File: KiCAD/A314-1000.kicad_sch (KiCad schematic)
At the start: 89 parts, among them IC1 T8Q144xx, IC2 SN74CBTD3384CPWR, IC3 SN74CBTD3384CPWR, IC4 SN74CBTD3384CPWR, IC5 SN74CBTD3384CPWR, IC6 IS61WV12816EDBLL-10TLI, IC7 LM1117MP-1.2, IC8 LM1117MP-3.3, J1 Raspberry_Pi_2_3, J2 2x30 Card edge conn., J3 Conn_01x01, J4 JTAG, Q1 2N7002, Q2 2N7002, U6 W25Q80DVSN, U7 TLV62569P, U8 TLV62569P, X1 25MHz

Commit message: Ready for production?
Board finished, added a RTC for the RPi. With a little luck and some production files, this may be ready for some PCBA :)
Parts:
- removed R3: 442k, Resistor_SMD:R_0603_1608Metric, symbol Device:R
- added BT1: CR2032, A314-1000:BATHLD001, symbol Device:Battery_Cell
- added C47: 100n, Capacitor_SMD:C_0603_1608Metric, symbol Device:C
- added C48, C49: 8p, Capacitor_SMD:C_0402_1005Metric_Pad0.74x0.62mm_HandSolder, symbol Device:C
- added FID1, FID2, FID3: Fiducial, Fiducial:Fiducial_1mm_Mask2mm, symbol Mechanical:Fiducial
- added IC11: PT7C4311WEX, Package_SO:SOIC-8_3.9x4.9mm_P1.27mm, symbol PT7C4311:PT7C4311
- added R17, R23: 3k9, Resistor_SMD:R_0603_1608Metric, symbol Device:R
- added Y1: 32.768kHz, Crystal:Crystal_DS26_D2.0mm_L6.0mm_Horizontal_1EP_style2, symbol Device:Crystal_GND3_Small
- J3: value Conn_01x01 -> INT2
- renumbered U6 to IC12
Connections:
- net INT2 is gone; now on an unnamed net: Q1.1 (G)
- net +3V3: now also C47.1, IC11.8 (V_{cc}), R17.2, R23.2
- net GND: now also BT1.2 (-), C47.2, C48.2, C49.2, IC11.4 (GND), Y1.3
- net JTAG_OE_{0}: now also J1.5 (SCL/GPIO3); no longer J1.37 (GPIO26)
- net JTAG_OE_{1}: now also J1.3 (SDA/GPIO2); no longer J1.13 (GPIO27)
- net PIACK: now also IC1.100 (GPIOR_113/CDI22); no longer IC1.101 (GPIOR_112/CDI23)
- net PIA_{0}: now also IC1.101 (GPIOR_112/CDI23), J1.18 (GPIO24); no longer IC1.111 (GPIOR_85), J1.27 (ID_SD/GPIO0)
- net PIA_{1}: now also IC1.103 (GPIOR_104/CDI25), J1.22 (GPIO25); no longer IC1.110 (GPIOR_87/CDI29), IC5.20 (2B4), J1.28 (ID_SC/GPIO1)
- net PIA_{2}: now also IC1.118 (GPIOR_79/ExtFB1/CDI30), J1.37 (GPIO26); no longer IC1.89 (GPIOR_129/CTRL10), J1.3 (SDA/GPIO2)
- net PIA_{3}: now also IC1.98 (GPIOR_117/CTRL14), J1.13 (GPIO27); no longer IC1.90 (GPIOR_128/CTRL11), J1.5 (SCL/GPIO3)
- net PID_{0}: now also IC1.90 (GPIOR_128/CTRL11); no longer IC1.93 (GPIOR_123/CLK12/CDI20)
- net PID_{10}: now also IC1.89 (GPIOR_129/CTRL10); no longer IC1.92 (GPIOR_125/CLK10)
- net PID_{11}: now also IC1.92 (GPIOR_125/CLK10); no longer IC1.97 (GPIOR_122/CLK13/CDI21)
- net PID_{12}: now also IC1.115 (GPIOR_82); no longer IC1.116 (GPIOR_81/MrefCLK)
- net PID_{13}: now also IC1.97 (GPIOR_122/CLK13/CDI21); no longer IC1.99 (GPIOR_116/CTRL15)
- net PID_{14}: now also IC1.93 (GPIOR_123/CLK12/CDI20); no longer IC1.98 (GPIOR_117/CTRL14)
- net PID_{15}: now also IC1.116 (GPIOR_81/MrefCLK); no longer IC1.117 (GPIOR_80)
- net PID_{1}: now also IC1.111 (GPIOR_85), IC5.20 (2B4); no longer IC1.112 (GPIOR_86)
- net PID_{2}: now also IC1.113 (GPIOR_84); no longer IC1.114 (GPIOR_83)
- net PID_{3}: now also IC1.110 (GPIOR_87/CDI29); no longer IC1.109 (GPIOR_88/CDI28)
- net PID_{4}: now also IC1.106 (GPIOR_94/CDI27); no longer IC1.105 (GPIOR_95/CDI26)
- net PID_{5}: now also IC1.105 (GPIOR_95/CDI26); no longer IC1.103 (GPIOR_104/CDI25)
- net PID_{7}: now also IC1.109 (GPIOR_88/CDI28); no longer IC1.106 (GPIOR_94/CDI27)
- net PID_{8}: now also IC1.112 (GPIOR_86); no longer IC1.113 (GPIOR_84)
- net PID_{9}: now also IC1.114 (GPIOR_83); no longer IC1.115 (GPIOR_82)
- net PIIRQ: now also IC1.99 (GPIOR_116/CTRL15); no longer IC1.100 (GPIOR_113/CDI22)
- net PIWR: now also IC1.117 (GPIOR_80); no longer IC1.118 (GPIOR_79/ExtFB1/CDI30)
- net 1V2PG: now reaches R6.1, U7.1 (EN), U8.5 (PG)
- new net: BT1.1 (+), IC11.3 (V_{bat})
- new net: C49.1, IC11.1 (X1), Y1.1
- new net: C48.1, IC11.2 (X2), Y1.2
- new net: IC11.5 (SDA), J1.27 (ID_SD/GPIO0), R17.1
- new net: IC11.6 (SCL), J1.28 (ID_SC/GPIO1), R23.1
- no-connect marks 11 -> 12
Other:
- moved on the sheet: C1, C12, C2, C3, C4, J3, Q1

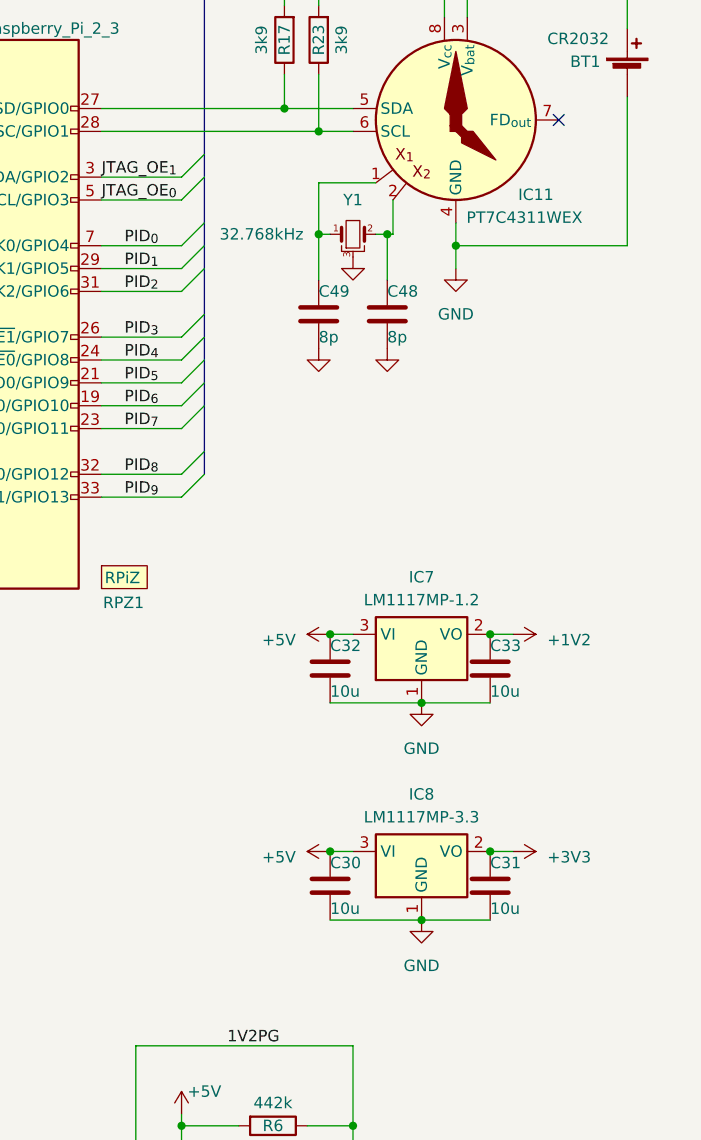
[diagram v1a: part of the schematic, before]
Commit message: Simplified PSU
Enhanced battery replacement ergonomics
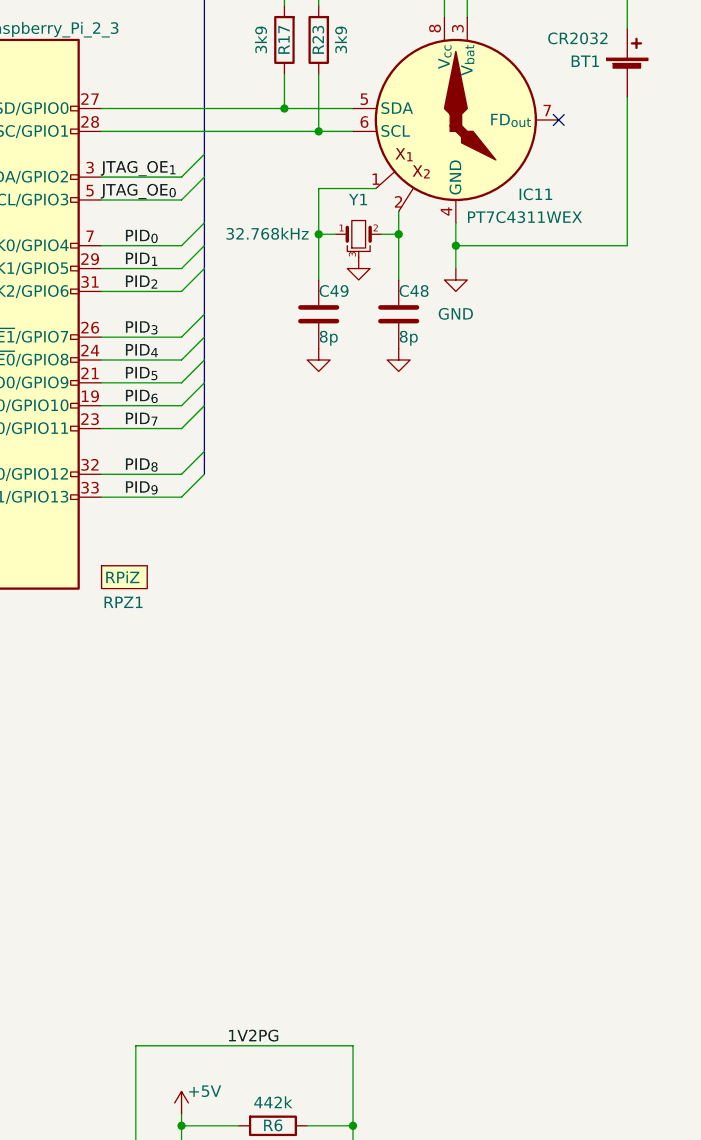
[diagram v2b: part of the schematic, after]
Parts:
- removed C30, C31, C32, C33: 10u, Capacitor_SMD:C_0603_1608Metric_Pad1.08x0.95mm_HandSolder, symbol Device:C
- removed IC7: LM1117MP-1.2, Package_TO_SOT_SMD:SOT-223-3_TabPin2, symbol a314-1000_components:LM1117MP-1.2
- removed IC8: LM1117MP-3.3, Package_TO_SOT_SMD:SOT-223-3_TabPin2, symbol Regulator_Linear:LM1117MP-3.3
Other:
- moved on the sheet: C48, Y1

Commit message: First bug-ridded release
This is the first non-alpha release. The hardware issues that were found in the alpha have been addressed. This board is now sent for a second production run.
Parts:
- added H1, H2: MountingHole, A314-1000:M2.5_Mount, symbol Mechanical:MountingHole
- added J5: RASP_I2C, Connector_PinHeader_2.54mm:PinHeader_1x05_P2.54mm_Vertical, symbol Connector_Generic:Conn_01x05
- added R24: 10k, Resistor_SMD:R_0603_1608Metric, symbol Device:R
- added R25: 3k9, Resistor_SMD:R_0603_1608Metric, symbol Device:R
- BT101: renamed from BT1; LCSC Part # (none) -> C964833
- C1, C10, C11, C12, C13, C14, C15, C16, C17, C18, C19, C2, C20, C21, C22, C23, C24, C25, C26, C27, C28, C29, C3, C4, C44, C45, C46, C5, C6, C7, C8, C9: LCSC Part # (none) -> C14663
- C10, C11, C12, C15, C16, C17: LCSC Part # (none) -> C19702
- C101: renamed from C48; LCSC Part # (none) -> C130118
- C102: renamed from C49; LCSC Part # (none) -> C130118
- C103: renamed from C47; LCSC Part # (none) -> C14663
- C13, C14: LCSC Part # (none) -> C19666
- FID1, FID2, FID3, J2: now left out of the parts list
- IC1: LCSC Part # (none) -> C5246494
- IC101: renamed from IC11; LCSC Part # (none) -> C780886
- IC12: LCSC Part # (none) -> C115408
- IC2, IC3, IC4, IC5: LCSC Part # (none) -> C2674525
- IC6: LCSC Part # (none) -> C1351846
- J1: LCSC Part # (none) -> C2685112
- J3: LCSC Part # (none) -> C2685179
- J4: now not fitted; now left out of the parts list
- L1, L2: LCSC Part # (none) -> C2847469
- Q1, Q2: LCSC Part # (none) -> C8545
- R1: value 6 x 10k -> 10k; LCSC Part # (none) -> C304474
- R10, R11, R12, R13, R14, R15, R2, R3, R4, R5, R6, R8, R9: LCSC Part # (none) -> C304474
- R17, R23: LCSC Part # (none) -> C103605
- R4, R6: LCSC Part # (none) -> C101050
- R4: LCSC Part # (none) -> C144686
- R5, R7, R8: LCSC Part # (none) -> C912480
- R7: value 4 x 10k -> 10k; LCSC Part # (none) -> C304474
- RPZ1: now not fitted
- U7, U8: LCSC Part # (none) -> C398365
- X1: LCSC Part # (none) -> C254248
- Y101: renamed from Y1; LCSC Part # (none) -> C511702
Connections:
- net +3V3: now also J5.2 (Pin_2), R24.2
- net +5V: now also J5.5 (Pin_5)
- net GND: now also J5.1 (Pin_1), R25.1
- net SPI_SS: now also R24.1
- net ~{CRESET}: now also U7.5 (PG)
- net SDA: now reaches IC101.5 (SDA), J1.27 (ID_SD/GPIO0), R17.1
- net SDA: now also J5.4 (Pin_4)
- net SCL: now reaches IC101.6 (SCL), J1.28 (ID_SC/GPIO1), R23.1
- net SCL: now also J5.3 (Pin_3)
- net at IC1.123 (GPIOR_77/PLLIN1), Q1.1 (G): now also R25.2
- no-connect marks 12 -> 14
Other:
- note added: "4 x"
- note added: "6 x"
- note added: "Components with designators 1xx are optional"
- moved on the sheet: C103, FID1, FID2, FID3, IC1F, R17, R23
